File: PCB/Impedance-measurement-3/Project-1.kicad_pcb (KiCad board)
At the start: 2 copper layers, 171 x 114 mm, 73 parts, among them U1 STM32F303CCT6

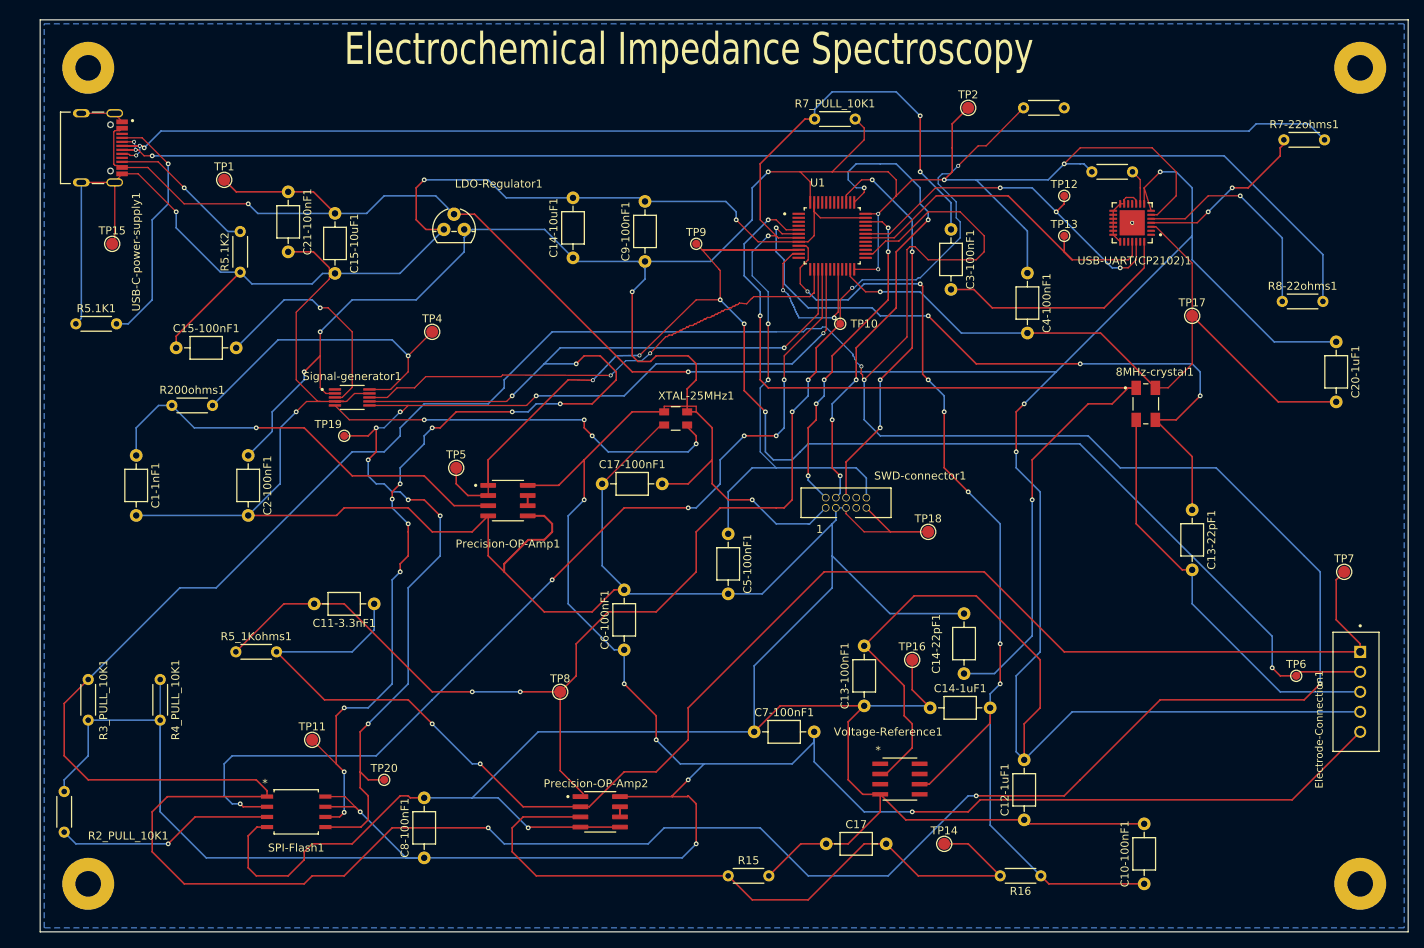
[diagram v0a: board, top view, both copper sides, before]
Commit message: schematic and layout changed 7/7/2026
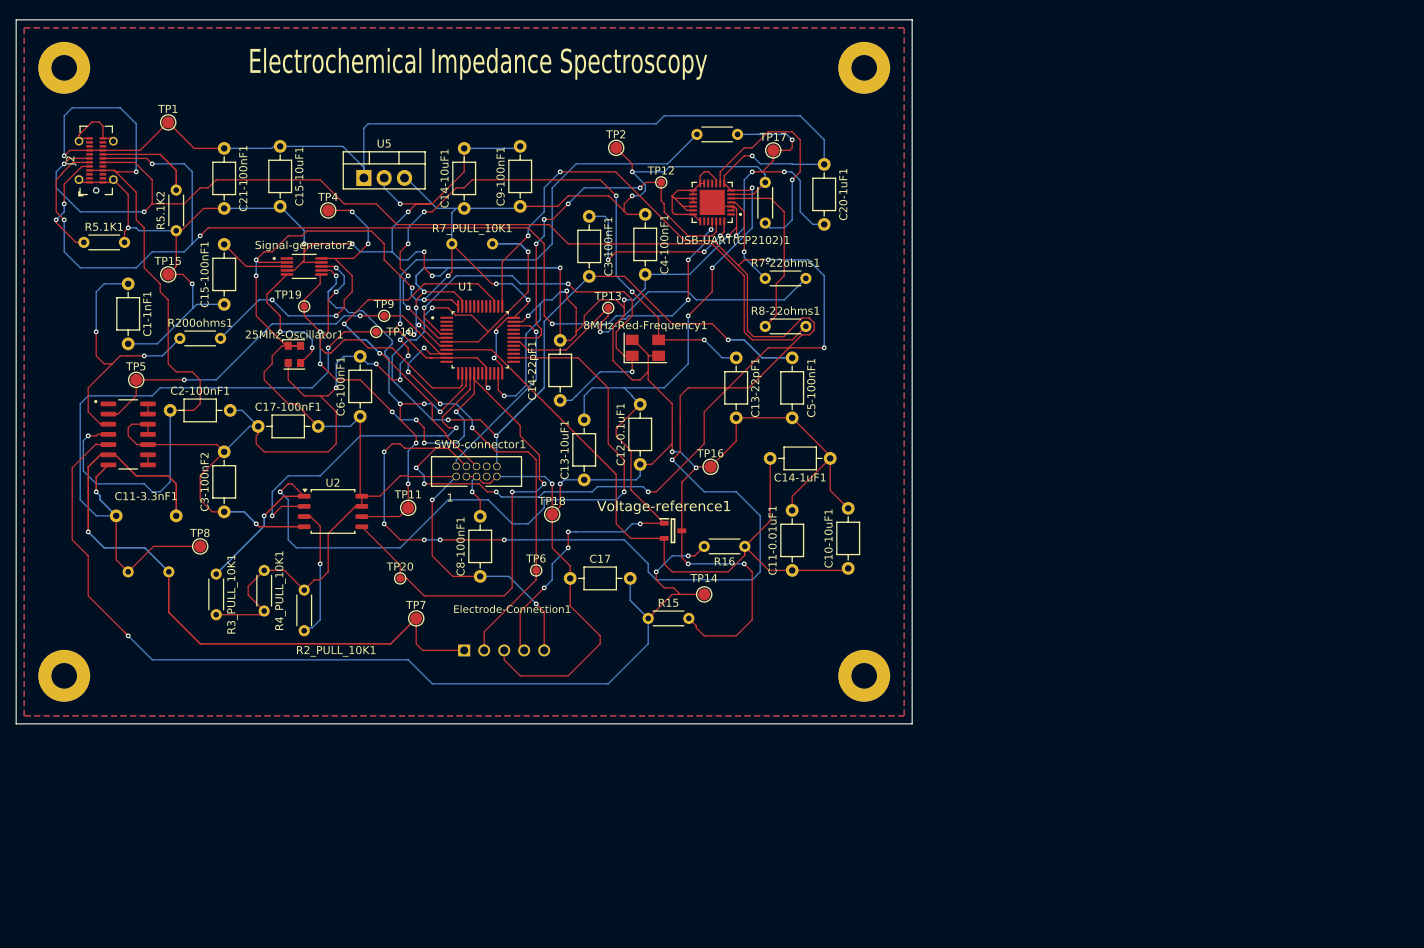
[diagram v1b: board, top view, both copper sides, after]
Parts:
- removed 8MHz-crystal1: ABM3B-8.000MHZ-B2-T, Symbol:XTAL_ABM3B-8.000MHZ-B2-T
- removed C7-100nF1: 100nF, Capacitor_THT:C_Axial_L3.8mm_D2.6mm_P7.50mm_Horizontal
- removed LDO-Regulator1: MCP1700, Symbol:TO92
- removed Precision-OP-Amp1, Precision-OP-Amp2: OPA2140AID, Symbol:SOIC127P599X175-8N
- removed the REF** at (67.0, 138.0)
- removed the REF** at (226.0, 138.0)
- removed the REF** at (67.0, 36.0)
- removed the REF** at (226.0, 36.0)
- removed SPI-Flash1: W25Q32JVSSIQ, Symbol:SOIC-8_5P28X5P28_WIN
- removed Signal-generator1: AD9833, Symbol:SOP50P490X110-10N
- removed USB-C-power-supply1: USB-C, Symbol:HRO_TYPE-C-31-M-12
- removed Voltage-Reference1: ADR4533BRZ, Symbol:R_8_ADI
- removed XTAL-25MHz1: ASE-25.000MHZ-LC-T, Symbol:CHIP_ASE-24_ABR
- added 25Mhz-Oscillator1: XO32, Oscillator:Oscillator_SMD_EuroQuartz_XO32-4Pin_3.2x2.5mm, F.Cu at (92.8, 71.8)
- added 8MHz-Red-Frequency1: Crystal_GND24, Crystal:Crystal_SMD_5032-4Pin_5.0x3.2mm, F.Cu at (136.7, 71.0)
- added C11-0.01uF1: 0.01uF, Capacitor_THT:C_Axial_L3.8mm_D2.6mm_P7.50mm_Horizontal, F.Cu at (155.0, 98.8)
- added C3-100nF2: 100nF, Capacitor_THT:C_Axial_L3.8mm_D2.6mm_P7.50mm_Horizontal, F.Cu at (84.0, 91.5)
- added J2: USB_C_Receptacle, Connector_USB:USB_C_Receptacle_GCT_USB4115-03-C, F.Cu at (68.0, 47.6)
- added REF**: MountingHole_3.2mm_M3_Pad, MountingHole:MountingHole_3.2mm_M3_Pad, F.Cu at (164.0, 112.0)
- added REF**: MountingHole_3.2mm_M3_Pad, MountingHole:MountingHole_3.2mm_M3_Pad, F.Cu at (64.0, 112.0)
- added REF**: MountingHole_3.2mm_M3_Pad, MountingHole:MountingHole_3.2mm_M3_Pad, F.Cu at (64.0, 36.0)
- added REF**: MountingHole_3.2mm_M3_Pad, MountingHole:MountingHole_3.2mm_M3_Pad, F.Cu at (164.0, 36.0)
- added Signal-generator2: AD9833BRMZ, Symbol:SOP50P490X110-10N, F.Cu at (94.0, 60.8)
- added U2: W25Q32JVSSIQ, Package_SO:SOIC-8_5.23x5.23mm_P1.27mm, F.Cu at (97.6, 91.5)
- added U5: LM7805_TO220, Package_TO_SOT_THT:TO-220-3_Vertical, F.Cu at (101.5, 49.8)
- added U9: OPA4141AID, Symbol:SOIC127P600X175-14N, F.Cu at (72.0, 81.8)
- added Voltage-reference1: ISL21080CIH333Z-TK, Symbol:SOT95P237X112-3N, F.Cu at (140.1, 93.9)
- C10-10uF1: renamed from C10-100nF1; value 100nF -> 10uF
- C11-3.3nF1, Electrode-Connection1, R5_1Kohms1, R7_PULL_10K1: moved to B.Cu
- C12-0.1uF1: renamed from C12-1uF1; value 1uF -> 0.1uF
- C13-10uF1: renamed from C13-100nF1; value 100nF -> 10uF
- moved TP7 116.1 mm to (108.0, 104.8)
- moved Electrode-Connection1 106.6 mm to (119.0, 108.3), turned to 180 degrees
- moved TP6 95.9 mm to (123.0, 98.8)
- moved C20-1uF1 67.7 mm to (159.0, 48.1)
- moved R7-22ohms1 67.1 mm to (151.6, 62.3)
- moved C12-0.1uF1 65.4 mm to (136.0, 85.6)
- moved R8-22ohms1 64.7 mm to (151.6, 68.3)
- moved C14-22pF1 60.9 mm to (126.0, 77.6)
- moved C13-22pF1 60.1 mm to (148.0, 72.2)
- moved TP10 58.0 mm to (103.0, 69.0)
- moved TP13 57.7 mm to (132.0, 66.0)
- moved TP17 56.3 mm to (152.6, 46.3)
- moved R16 55.4 mm to (149.1, 95.8)
- moved C10-10uF1 54.1 mm to (162.0, 98.6)
- moved USB-UART(CP2102)1 52.6 mm to (145.0, 52.8)
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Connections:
- net Net-(SPI-Flash1-/CS) renamed /M-PB13
- net Net-(U1-PA10) renamed /USB-TXD
- net Net-(U1-PA9) renamed /USB-RXD
- net Net-(U1-VDDA/VREF+) renamed /M-VREF+
- C12-0.1uF1 pad 2: VBUS -> /VBUS-5V
- C13-10uF1 pad 2: VBUS -> /VBUS-5V
- C15-10uF1 pad 1: VBUS -> /VBUS-5V
- C2-100nF1 pad 1: VDD -> /VBUS-5V
- C20-1uF1 pad 1: VBUS -> /VBUS-5V
- C21-100nF1 pad 1: VBUS -> /VBUS-5V
- C3-100nF1 pad 1: Net-(SWD-connector1-RESET) -> Net-(USB-UART(CP2102)1-DTR)
- C3-100nF1 pad 2: Net-(USB-UART(CP2102)1-DTR) -> /M-NRST
- C5-100nF1 pad 1: Net-(SWD-connector1-RESET) -> /M-NRST
- Electrode-Connection1 pad 4: VBUS -> /VBUS-5V
- R5.1K1 pad 1: GND -> Net-(J2-CC1)
- R5.1K1 pad 2: Net-(USB-C-power-supply1-CC1) -> GND
- R7_PULL_10K1 pad 1: Net-(SWD-connector1-RESET) -> /M-NRST
- SWD-connector1 pad 10: Net-(SWD-connector1-RESET) -> /M-NRST
- TP1 pad 1: VBUS -> /VBUS-5V
- U1 pad 16: Net-(SPI-Flash1-DO(IO1)) -> /M-PA6
- U1 pad 7: Net-(SWD-connector1-RESET) -> /M-NRST
- USB-UART(CP2102)1 pad 7: VBUS -> /VBUS-5V
- USB-UART(CP2102)1 pad 8: VBUS -> /VBUS-5V
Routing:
- net VBUS: track 378.9 -> 0.00 mm, vias 5 -> 0
- net /M-PB13: track 477.2 -> 101.8 mm, vias 5 -> 3
- net VDD: track 606.4 -> 269.2 mm, vias 16 -> 13
- net /VBUS-5V: track 0.00 -> 320.4 mm, vias 0 -> 11
- net Net-(SWD-connector1-SWDCLK): track 61.2 -> 276.1 mm, vias 5 -> 14
- net GND: track 780.0 -> 578.1 mm, vias 7 -> 36
- net Net-(SPI-Flash1-DO(IO1)): track 120.9 -> 0.00 mm, vias 6 -> 0
- net /M-NRST: track 0.00 -> 116.6 mm, vias 0 -> 5
- net Net-(SWD-connector1-RESET): track 114.2 -> 0.00 mm, vias 5 -> 0
- net Net-(Signal-generator2-SCLK): track 166.6 -> 58.5 mm, vias 13 -> 6
- net /Electrode2: track 190.4 -> 85.9 mm, vias 2 -> 1
- net /Electrode1: track 195.3 -> 105.1 mm
- net Net-(U1-PF0/OSC_IN): track 123.0 -> 55.5 mm
- net Net-(Signal-generator1-MCLK): track 51.4 -> 0.00 mm, vias 4 -> 0
- net /M-VREF+: track 131.3 -> 82.8 mm, vias 7 -> 0
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- added copper zone on F.Cu, net VDD
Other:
- board size 171 x 114 mm -> 112 x 88 mm
